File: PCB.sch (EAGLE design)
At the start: 43 parts, among them IC1 PIC16F1826/27SO, IC2 MAX3467CPA, U1 +12v, Y1 ASL-16.000MHZ-L-C-S-50-T

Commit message: Switching to make D9 for power input
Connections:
- net RXN: now also X4.8; no longer X4.7
- net RXP: now also X4.4; no longer X4.2
- net TXN: now also X4.7; no longer X4.8
- net TXP: now also X4.2; no longer X4.4
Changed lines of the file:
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@@
 <segment>
 <pinref part="IC2" gate="G$1" pin="A"/>
-<wire x1="-73.66" y1="25.4" x2="-91.44" y2="25.4" width="0.1524" layer="91"/>
-<wire x1="-91.44" y1="25.4" x2="-91.44" y2="33.02" width="0.1524" layer="91"/>
-<pinref part="X4" gate="-1" pin="2"/>
-<wire x1="-91.44" y1="33.02" x2="-96.52" y2="33.02" width="0.1524" layer="91"/>
+<wire x1="-73.66" y1="25.4" x2="-88.9" y2="25.4" width="0.1524" layer="91"/>
+<pinref part="X4" gate="-1" pin="4"/>
+<wire x1="-96.52" y1="27.94" x2="-88.9" y2="27.94" width="0.1524" layer="91"/>
+<wire x1="-88.9" y1="27.94" x2="-88.9" y2="25.4" width="0.1524" layer="91"/>
 </segment>
 </net>
@@
 <segment>
 <pinref part="IC2" gate="G$1" pin="B"/>
-<wire x1="-73.66" y1="20.32" x2="-88.9" y2="20.32" width="0.1524" layer="91"/>
-<pinref part="X4" gate="-1" pin="7"/>
+<wire x1="-73.66" y1="20.32" x2="-86.36" y2="20.32" width="0.1524" layer="91"/>
 <pinref part="JP2" gate="G$1" pin="1"/>
-<wire x1="-68.58" y1="55.88" x2="-88.9" y2="55.88" width="0.1524" layer="91"/>
-<wire x1="-88.9" y1="55.88" x2="-88.9" y2="40.64" width="0.1524" layer="91"/>
-<wire x1="-88.9" y1="40.64" x2="-88.9" y2="20.32" width="0.1524" layer="91"/>
-<wire x1="-111.76" y1="33.02" x2="-121.92" y2="33.02" width="0.1524" layer="91"/>
-<wire x1="-121.92" y1="33.02" x2="-121.92" y2="40.64" width="0.1524" layer="91"/>
-<wire x1="-121.92" y1="40.64" x2="-88.9" y2="40.64" width="0.1524" layer="91"/>
-<junction x="-88.9" y="40.64"/>
+<wire x1="-68.58" y1="55.88" x2="-86.36" y2="55.88" width="0.1524" layer="91"/>
+<wire x1="-86.36" y1="55.88" x2="-86.36" y2="20.32" width="0.1524" layer="91"/>
+<wire x1="-86.36" y1="20.32" x2="-119.38" y2="20.32" width="0.1524" layer="91"/>
+<wire x1="-119.38" y1="20.32" x2="-119.38" y2="30.48" width="0.1524" layer="91"/>
+<junction x="-86.36" y="20.32"/>
+<pinref part="X4" gate="-1" pin="8"/>
+<wire x1="-119.38" y1="30.48" x2="-111.76" y2="30.48" width="0.1524" layer="91"/>
 </segment>
 </net>
@@
 <pinref part="IC2" gate="G$1" pin="Z"/>
 <wire x1="-73.66" y1="30.48" x2="-81.28" y2="30.48" width="0.1524" layer="91"/>
-<pinref part="X4" gate="-1" pin="8"/>
 <pinref part="JP1" gate="G$1" pin="1"/>
 <wire x1="-68.58" y1="66.04" x2="-81.28" y2="66.04" width="0.1524" layer="91"/>
 <wire x1="-81.28" y1="66.04" x2="-81.28" y2="43.18" width="0.1524" layer="91"/>
+<pinref part="X4" gate="-1" pin="7"/>
 <wire x1="-81.28" y1="43.18" x2="-81.28" y2="30.48" width="0.1524" layer="91"/>
-<wire x1="-111.76" y1="30.48" x2="-124.46" y2="30.48" width="0.1524" layer="91"/>
-<wire x1="-124.46" y1="30.48" x2="-124.46" y2="43.18" width="0.1524" layer="91"/>
-<wire x1="-124.46" y1="43.18" x2="-81.28" y2="43.18" width="0.1524" layer="91"/>
+<wire x1="-111.76" y1="33.02" x2="-119.38" y2="33.02" width="0.1524" layer="91"/>
+<wire x1="-119.38" y1="33.02" x2="-119.38" y2="43.18" width="0.1524" layer="91"/>
+<wire x1="-119.38" y1="43.18" x2="-81.28" y2="43.18" width="0.1524" layer="91"/>
 <junction x="-81.28" y="43.18"/>
 </segment>
@@
 <segment>
 <pinref part="IC2" gate="G$1" pin="Y"/>
-<wire x1="-73.66" y1="35.56" x2="-86.36" y2="35.56" width="0.1524" layer="91"/>
-<wire x1="-86.36" y1="35.56" x2="-86.36" y2="27.94" width="0.1524" layer="91"/>
-<pinref part="X4" gate="-1" pin="4"/>
-<wire x1="-86.36" y1="27.94" x2="-96.52" y2="27.94" width="0.1524" layer="91"/>
+<wire x1="-73.66" y1="35.56" x2="-83.82" y2="35.56" width="0.1524" layer="91"/>
+<wire x1="-83.82" y1="35.56" x2="-83.82" y2="33.02" width="0.1524" layer="91"/>
+<pinref part="X4" gate="-1" pin="2"/>
+<wire x1="-83.82" y1="33.02" x2="-96.52" y2="33.02" width="0.1524" layer="91"/>
 </segment>
 </net>

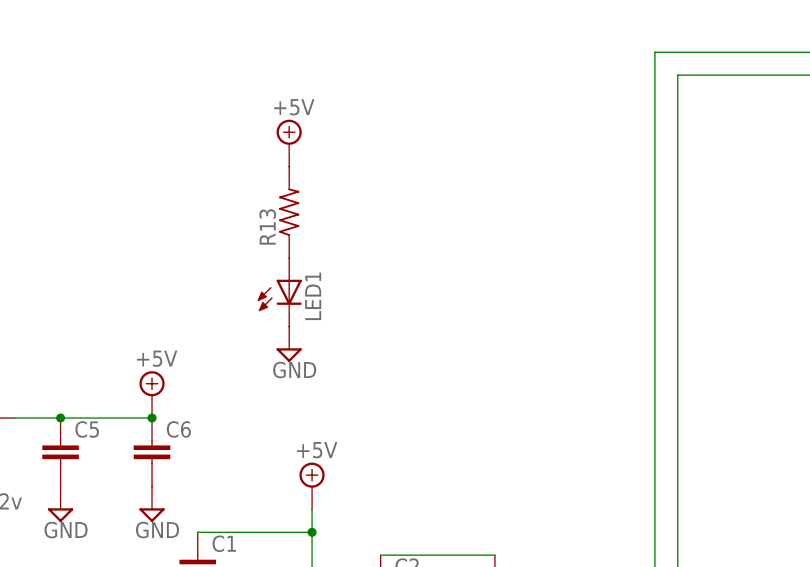
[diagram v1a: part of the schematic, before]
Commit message: Adding 5V TP
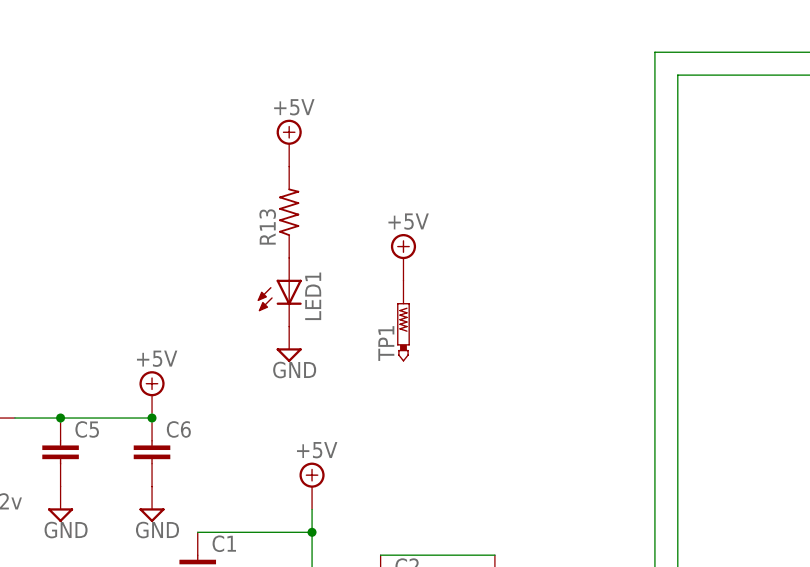
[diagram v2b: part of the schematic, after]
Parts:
- added TP1: PTR1PAD1-17, testpad:PTR1PAD1-17
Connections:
- net +5V: now also TP1.TP
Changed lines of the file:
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@@
 <part name="R15" library="resistor" deviceset="R-US_" device="M1206"/>
 <part name="SUPPLY57" library="supply2" deviceset="GND" device=""/>
+<part name="TP1" library="testpad" deviceset="PTR1" device="PAD1-17"/>
+<part name="SUPPLY58" library="supply2" deviceset="+5V" device=""/>
 </parts>
 <sheets>
@@
 <instance part="R15" gate="G$1" x="-2.54" y="-2.54" rot="R90"/>
 <instance part="SUPPLY57" gate="GND" x="-2.54" y="-10.16"/>
+<instance part="TP1" gate="G$1" x="35.56" y="119.38"/>
+<instance part="SUPPLY58" gate="+5V" x="35.56" y="124.46"/>
 </instances>
 <busses>
@@
 <pinref part="SUPPLY54" gate="+5V" pin="+5V"/>
 </segment>
-</net>
+<segment>
+<pinref part="TP1" gate="G$1" pin="TP"/>
+<pinref part="SUPPLY58" gate="+5V" pin="+5V"/>
+</segment>
+</net>

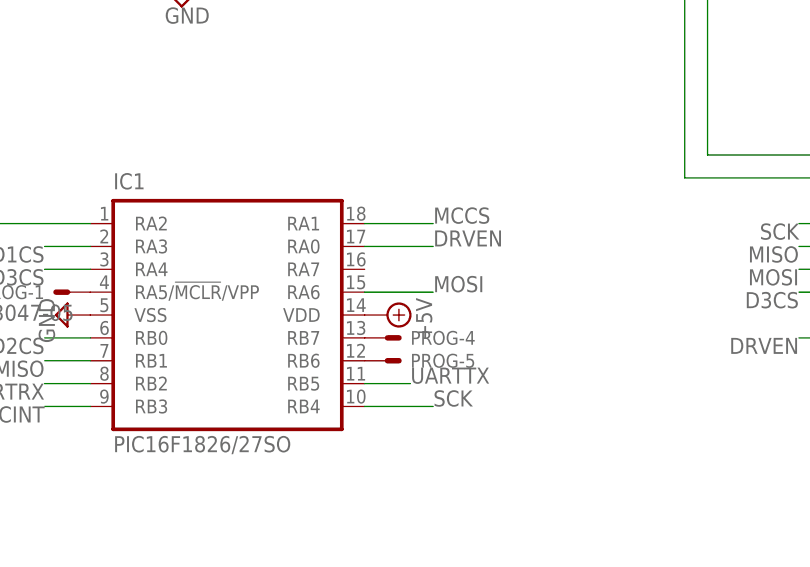
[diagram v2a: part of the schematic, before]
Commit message: Adding PIC test point
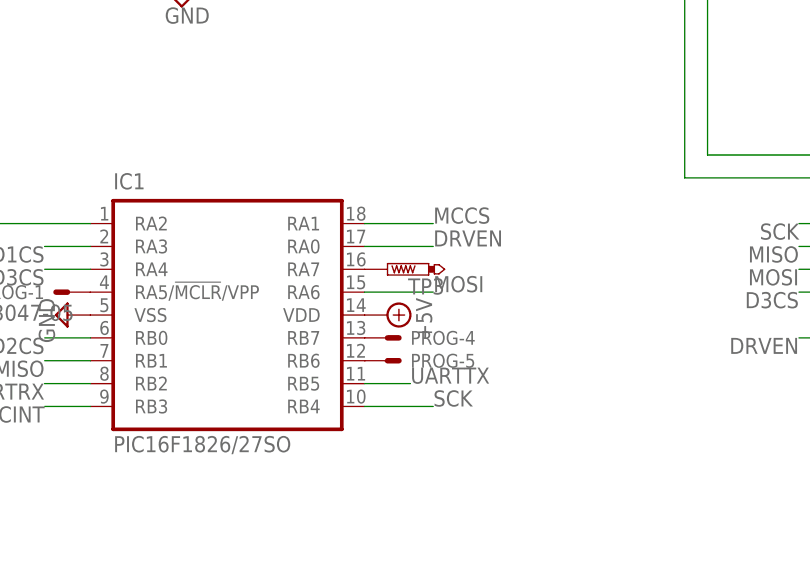
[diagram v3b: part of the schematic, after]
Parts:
- added TP3: PTR1B1,27, testpad:PTR1B1,27
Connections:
- new net N$25: IC1.RA7, TP3.TP
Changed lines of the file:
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@@
 <part name="TP1" library="testpad" deviceset="PTR1" device="PAD1-17"/>
 <part name="SUPPLY58" library="supply2" deviceset="+5V" device=""/>
+<part name="TP3" library="testpad" deviceset="PTR1" device="B1,27"/>
 </parts>
 <sheets>
@@
 <instance part="TP1" gate="G$1" x="35.56" y="119.38"/>
 <instance part="SUPPLY58" gate="+5V" x="35.56" y="124.46"/>
+<instance part="TP3" gate="G$1" x="50.8" y="-2.54" rot="R90"/>
 </instances>
 <busses>
@@
 </segment>
 </net>
+<net name="N$25" class="0">
+<segment>
+<pinref part="IC1" gate="G$1" pin="RA7"/>
+<pinref part="TP3" gate="G$1" pin="TP"/>
+</segment>
+</net>
